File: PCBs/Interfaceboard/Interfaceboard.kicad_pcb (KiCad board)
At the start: 2 copper layers, 80 x 80 mm, 68 parts, among them J301 TSW-105-07-T-D, J302 TSW-105-07-T-D, J304 TSW-105-07-T-D, J305 TSW-105-07-T-D, SW1 PTS645, SW2 PTS645, SW3 PTS645, SW4 PTS645, SW5 PTS645, U1 AD8420ARMZ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

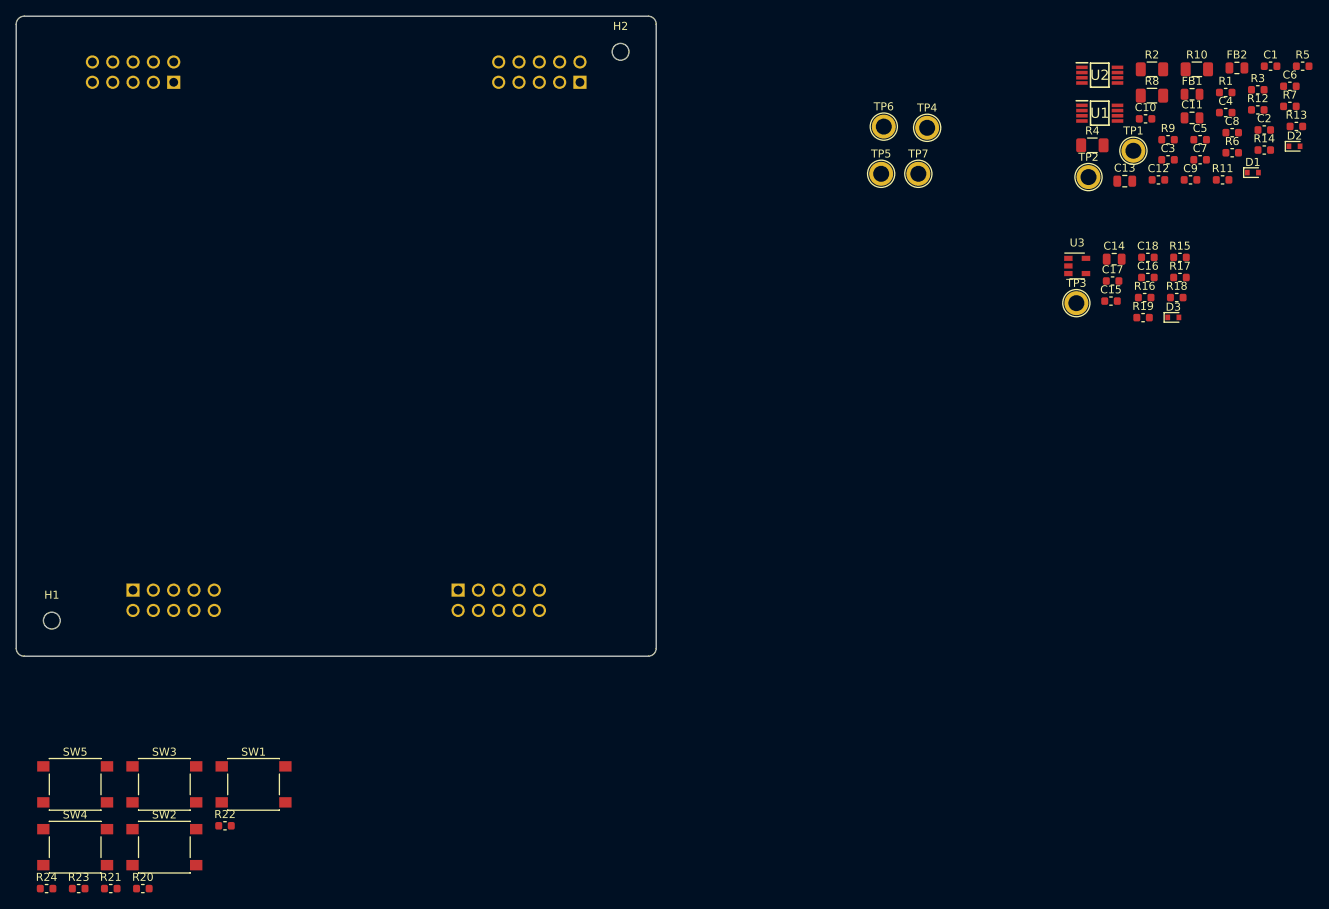
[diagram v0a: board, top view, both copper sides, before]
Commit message: Made changes to resistor sizes and footprints. Placed switches on PCB, ready for the rest.
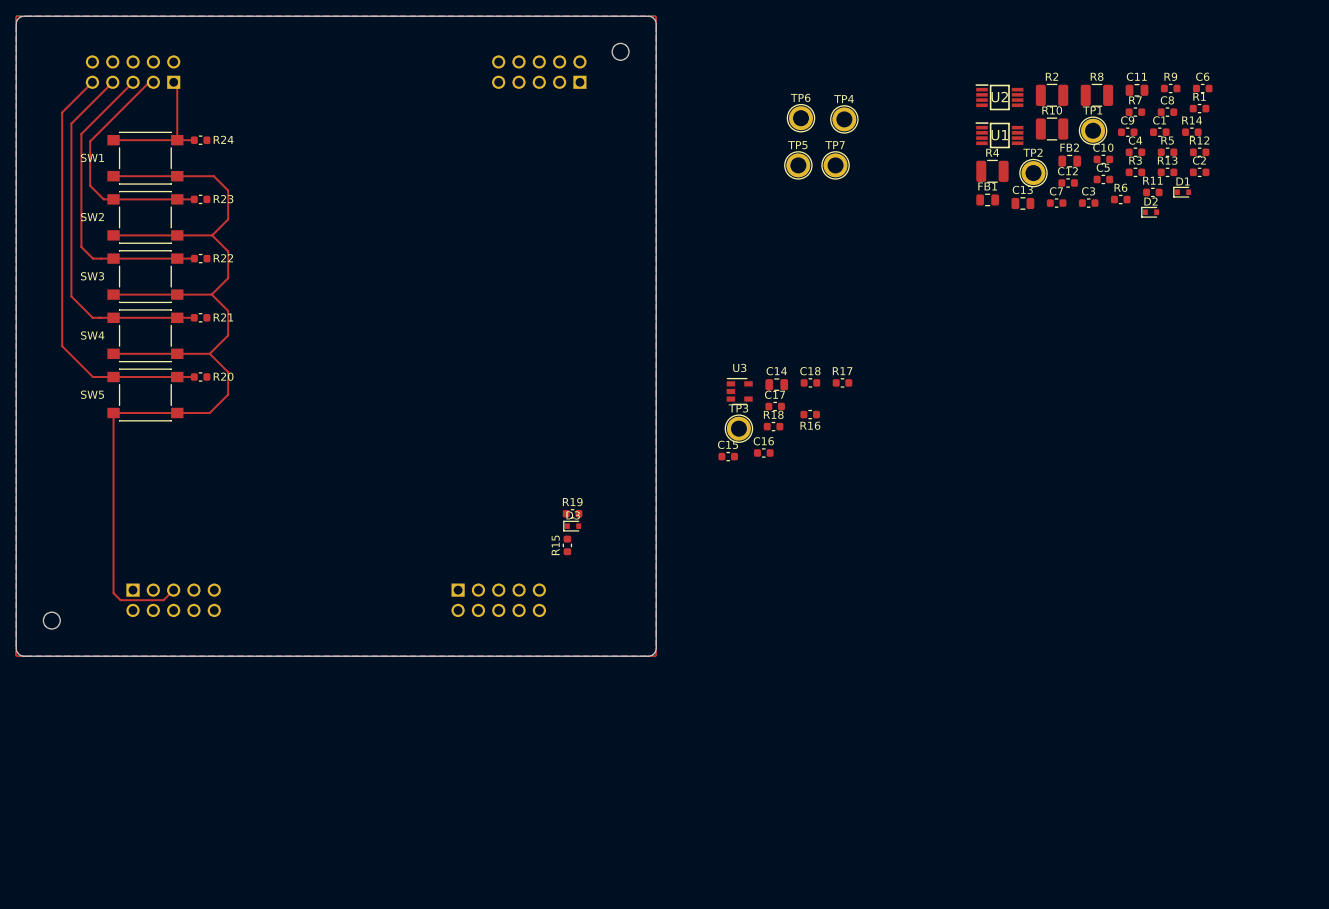
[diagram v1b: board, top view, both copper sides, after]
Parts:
- R10, R4: value sot -> 56; footprint Resistor_SMD:R_1206_3216Metric -> Resistor_SMD:R_1210_3225Metric
- R11, R5: value sot -> 3.09
- R12, R6: value sot -> DNP
- R15: value 9.88k -> 11.5k
- R2, R8: value sot -> 54.9; footprint Resistor_SMD:R_1206_3216Metric -> Resistor_SMD:R_1210_3225Metric
- moved R24 95.5 mm to (128.1, 65.5)
- moved R23 87.5 mm to (128.1, 72.9)
- moved R15 84.6 mm to (173.9, 116.2), turned to 90 degrees
- moved D3 79.4 mm to (174.6, 113.7)
- moved SW1 79.4 mm to (121.2, 67.8), turned to 180 degrees
- moved SW2 78.8 mm to (121.2, 75.2), turned to 180 degrees
- moved R19 75.4 mm to (174.6, 112.2)
- moved R21 72.2 mm to (128.1, 87.7)
- moved R22 71.0 mm to (128.1, 80.3)
- moved SW4 64.5 mm to (121.2, 90.0), turned to 180 degrees
- moved R20 64.4 mm to (128.1, 95.1)
- moved SW3 63.5 mm to (121.2, 82.5), turned to 180 degrees
- moved R18 52.9 mm to (199.7, 101.3)
- moved C16 52.8 mm to (198.4, 104.6)
- moved C15 51.6 mm to (194.0, 105.0)
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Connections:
- J301 pad 3: +3V3_Acc -> +5V_Ref
- J301 pad 5: +3V3_Acc -> +3V3_Ref
- R13 pad 2: +3V3_Acc -> +3V3_Ref
- R15 pad 1: +3V3_Acc -> +3V3_Ref
- SW1 pad 1: +3V3_Acc -> +3V3_Ref
- SW2 pad 1: +3V3_Acc -> +3V3_Ref
- SW3 pad 1: +3V3_Acc -> +3V3_Ref
- SW4 pad 1: +3V3_Acc -> +3V3_Ref
- SW5 pad 1: +3V3_Acc -> +3V3_Ref
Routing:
- net +3V3_Ref: track 0.00 -> 128.7 mm
- net /Buttons/Dig5: track 0.00 -> 52.7 mm
- net /Buttons/Dig4: track 0.00 -> 45.6 mm
- net /Buttons/Dig3: track 0.00 -> 38.0 mm
- net /Buttons/Dig2: track 0.00 -> 30.2 mm
- net /Buttons/Dig1: track 0.00 -> 17.5 mm
- added copper zone on B.Cu, net GND
- added copper zone on F.Cu, net GND

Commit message: Minor changes to schematics, removed test points, placed a few components on PCB.
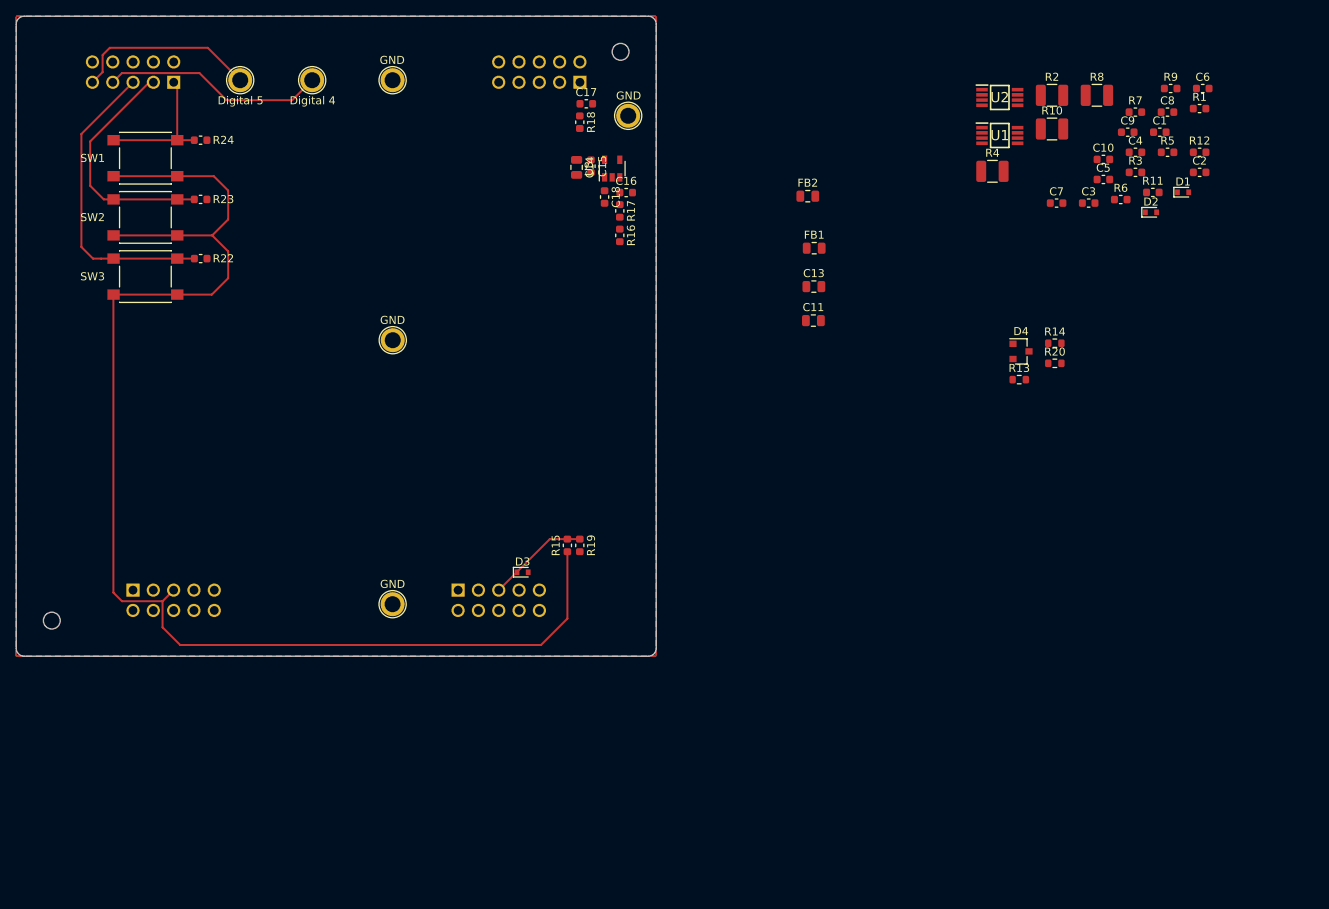
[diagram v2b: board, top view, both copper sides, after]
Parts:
- removed C12: 100n, Capacitor_SMD:C_0603_1608Metric
- removed R21: 10k, Resistor_SMD:R_0603_1608Metric
- removed SW4, SW5: PTS645, Button_Switch_SMD:SW_SPST_PTS645
- removed TP1, TP2, TP3: TestPoint, TestPoint:TestPoint_Plated_Hole_D2.0mm
- added D4: LM4041CFTA, ElectricGoKart:LM4041, F.Cu at (230.6, 91.9)
- added TP8: TestPoint, TestPoint:TestPoint_Plated_Hole_D2.0mm, F.Cu at (142.0, 58.0)
- added TP9: TestPoint, TestPoint:TestPoint_Plated_Hole_D2.0mm, F.Cu at (133.0, 58.0)
- R13: value 5.6k -> 5.1k
- R14: value 1k -> 1.43k
- R20: value 10k -> 1k
- moved R20 106.8 mm to (234.8, 93.4)
- moved TP6 79.4 mm to (152.1, 123.5)
- moved TP4 62.8 mm to (152.1, 90.5)
- moved TP7 56.4 mm to (152.1, 58.0)
- moved C11 49.6 mm to (204.7, 88.0)
- moved R18 45.1 mm to (175.4, 63.2), turned to 270 degrees
- moved C17 44.6 mm to (176.3, 61.0)
- moved C15 40.1 mm to (176.8, 68.8), turned to 270 degrees
- moved C14 36.9 mm to (175.1, 68.9), turned to 270 degrees
- moved C16 36.8 mm to (181.2, 72.0)
- moved R17 35.2 mm to (180.4, 74.3), turned to 270 degrees
- moved C18 34.7 mm to (178.6, 72.6), turned to 270 degrees
- moved FB2 33.0 mm to (203.9, 72.5)
- moved R16 32.7 mm to (180.4, 77.4), turned to 270 degrees
- moved U3 32.1 mm to (179.5, 69.0), turned to 90 degrees
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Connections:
- R13 pad 1: /Currents/0V5 -> Net-(D4-Pad1)
- R14 pad 1: GND -> /Currents/0V5
- R14 pad 2: /Currents/0V5 -> Net-(D4-Pad1)
- R20 pad 1: /Buttons/Dig5 -> GND
- R20 pad 2: GND -> /Currents/0V5
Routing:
- net +3V3_Ref: track 128.7 -> 165.5 mm
- net /Buttons/Dig5: track 52.7 -> 23.2 mm
- net /Buttons/Dig4: track 45.6 -> 27.8 mm
- net /Connectors/Torque_Meas: track 0.00 -> 12.8 mm
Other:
- board text added: "Digital 4"
- board text added: "Digital 5"
- board text added: "GND"

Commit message: Removed some buttons and added LEDs. Finished placing the components on the PCB.
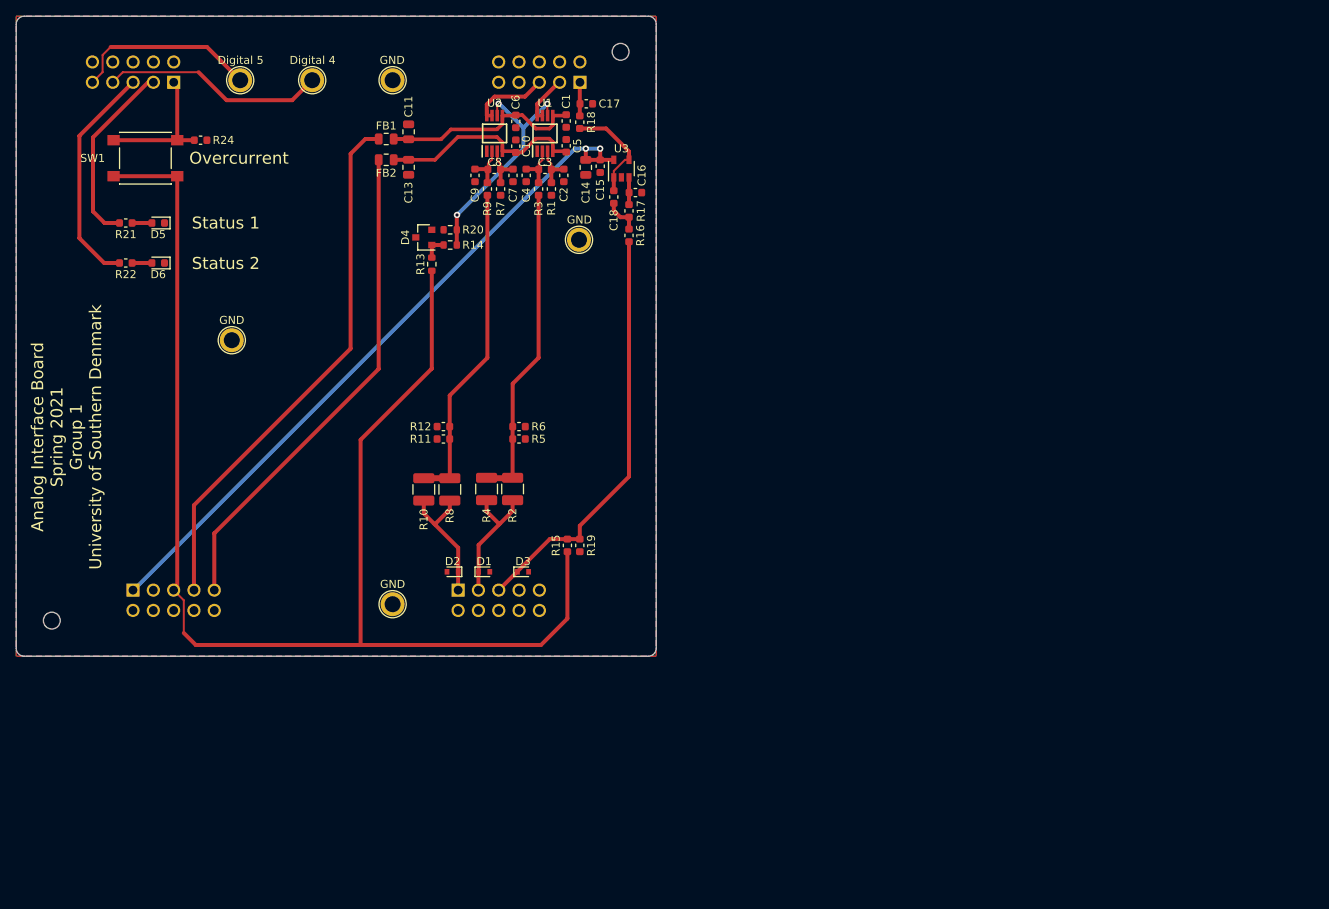
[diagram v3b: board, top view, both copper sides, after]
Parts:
- removed R23: 10k, Resistor_SMD:R_0603_1608Metric
- removed SW2, SW3: PTS645, Button_Switch_SMD:SW_SPST_PTS645
- added D5: 150060SS75000, LED_SMD:LED_0603_1608Metric, F.Cu at (122.8, 75.8)
- added D6: 150060VS75000, LED_SMD:LED_0603_1608Metric, F.Cu at (122.8, 80.8)
- added R21: 270, Resistor_SMD:R_0603_1608Metric, F.Cu at (118.7, 75.8)
- R22: value 10k -> 270
- moved R12 100.6 mm to (158.4, 101.3)
- moved D1 99.4 mm to (163.5, 119.5)
- moved D2 98.2 mm to (159.6, 119.5), turned to 180 degrees
- moved R8 94.7 mm to (159.2, 109.2), turned to 270 degrees
- moved R11 93.9 mm to (158.4, 102.8)
- moved R10 90.5 mm to (155.9, 109.2), turned to 270 degrees
- moved R5 88.6 mm to (167.8, 102.8), turned to 180 degrees
- moved R9 86.3 mm to (163.9, 71.6), turned to 270 degrees
- moved C6 86.0 mm to (167.4, 63.1), turned to 270 degrees
- moved C8 84.5 mm to (164.8, 69.2), turned to 180 degrees
- moved R2 83.5 mm to (167.1, 109.1), turned to 270 degrees
- moved C9 81.8 mm to (162.3, 69.9), turned to 270 degrees
- moved R1 81.6 mm to (171.9, 71.6), turned to 270 degrees
- moved R6 80.4 mm to (167.8, 101.3), turned to 180 degrees
- moved R7 79.9 mm to (165.6, 71.6), turned to 270 degrees
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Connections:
- D1 pad 1: /Currents/Phase1_In -> /Currents/Phase2_In
- D2 pad 1: /Currents/Phase2_In -> /Currents/Phase1_In
- R10 pad 2: /Currents/Phase2_In -> /Currents/Phase1_In
- R2 pad 2: /Currents/Phase1_In -> /Currents/Phase2_In
- R22 pad 1: /Buttons/Dig3 -> Net-(D6-Pad2)
- R22 pad 2: GND -> /Buttons/Dig3
- R4 pad 2: /Currents/Phase1_In -> /Currents/Phase2_In
- R8 pad 2: /Currents/Phase2_In -> /Currents/Phase1_In
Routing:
- net +5V: track 0.00 -> 87.6 mm, vias 0 -> 2
- net +15V: track 0.00 -> 66.9 mm
- net -15V: track 0.00 -> 62.3 mm
- net Net-(R10-Pad1): track 0.00 -> 40.6 mm
- net Net-(R2-Pad1): track 0.00 -> 39.9 mm
- net /Connectors/Torque_Meas: track 12.8 -> 52.5 mm
- net /Currents/0V5: track 0.00 -> 29.7 mm, vias 0 -> 3
- net /Currents/-15V_Filt: track 0.00 -> 26.3 mm
- net /Currents/+15V_Filt: track 0.00 -> 25.6 mm
- net /Currents/Phase1_In: track 0.00 -> 16.7 mm
- net /Currents/Phase2_In: track 0.00 -> 16.6 mm
- net Net-(C18-Pad1): track 0.00 -> 13.5 mm
- net /Connectors/ADC4: track 0.00 -> 9.76 mm
- net /Buttons/Dig3: track 38.0 -> 28.6 mm
- net +3V3_Ref: track 165.5 -> 174.6 mm
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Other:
- board text added: "Analog Interface Board Spring 2021 Group 1 University of Southern Denmark"
- board text added: "Overcurrent"
- board text added: "Status 1"
- board text added: "Status 2"
